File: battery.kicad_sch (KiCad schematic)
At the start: 22 parts, among them J1 Conn_01x04_Female, J10 Conn_01x06_Male, J11 Conn_01x02_Female, J2 Conn_02x05_Odd_Even, J3 Conn_02x03_Odd_Even, Q1 2N7002, Q10 Q_PMOS_GSD, Q2 Q_PMOS_GSD, U1 AP3428

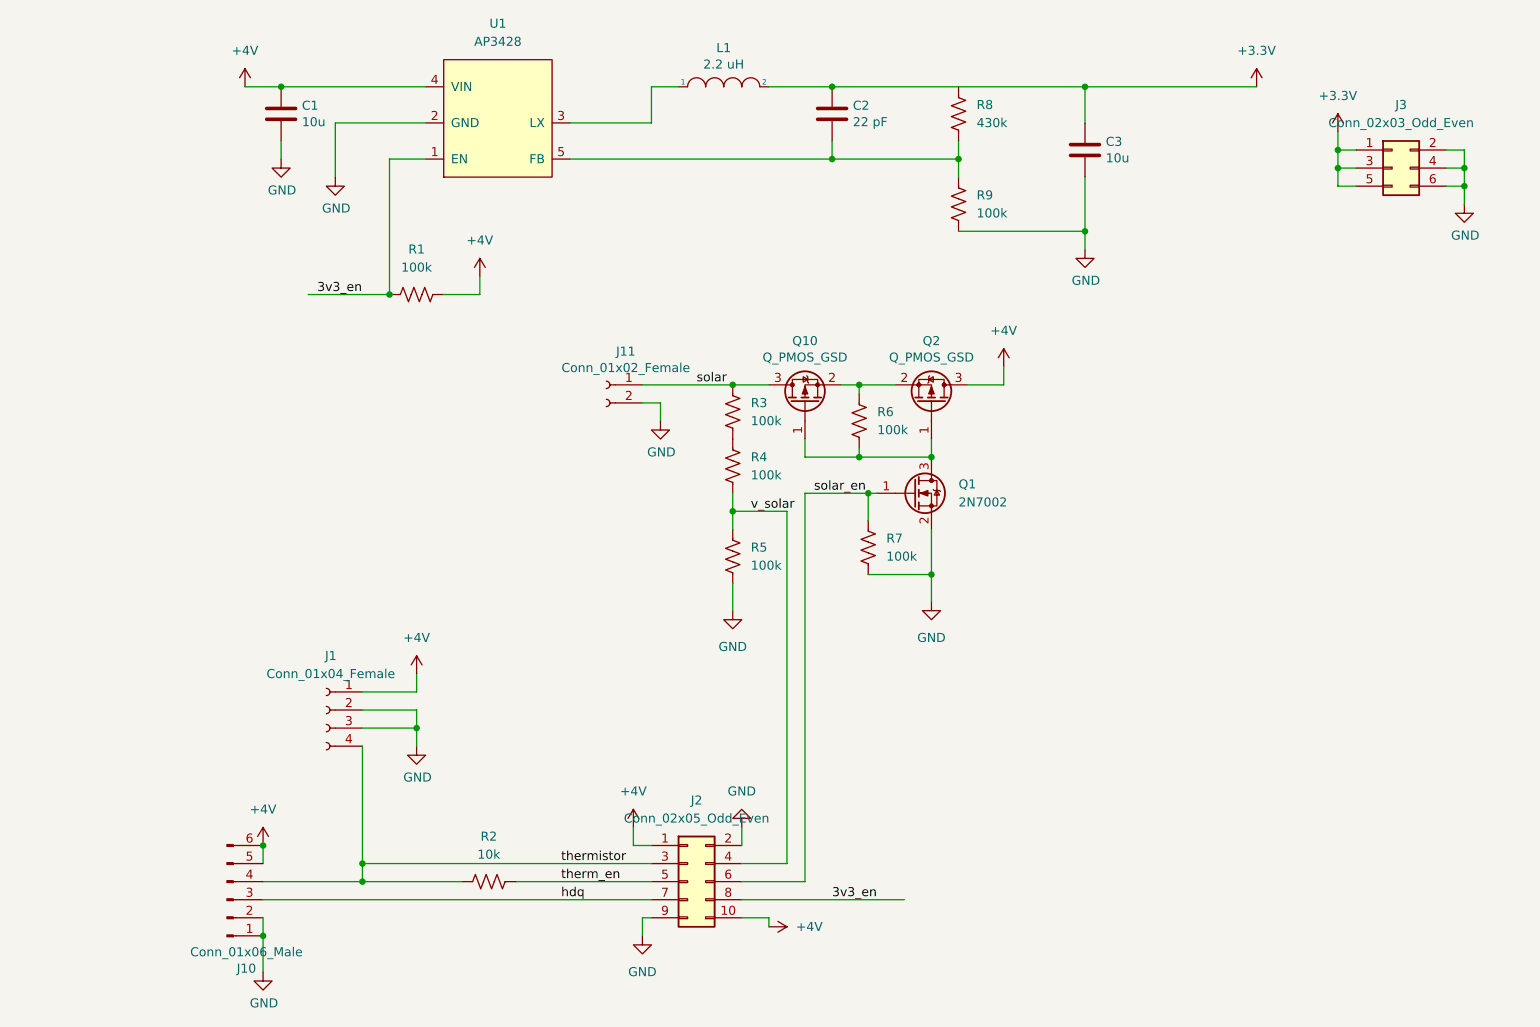
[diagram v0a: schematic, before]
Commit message: tight regulator layout
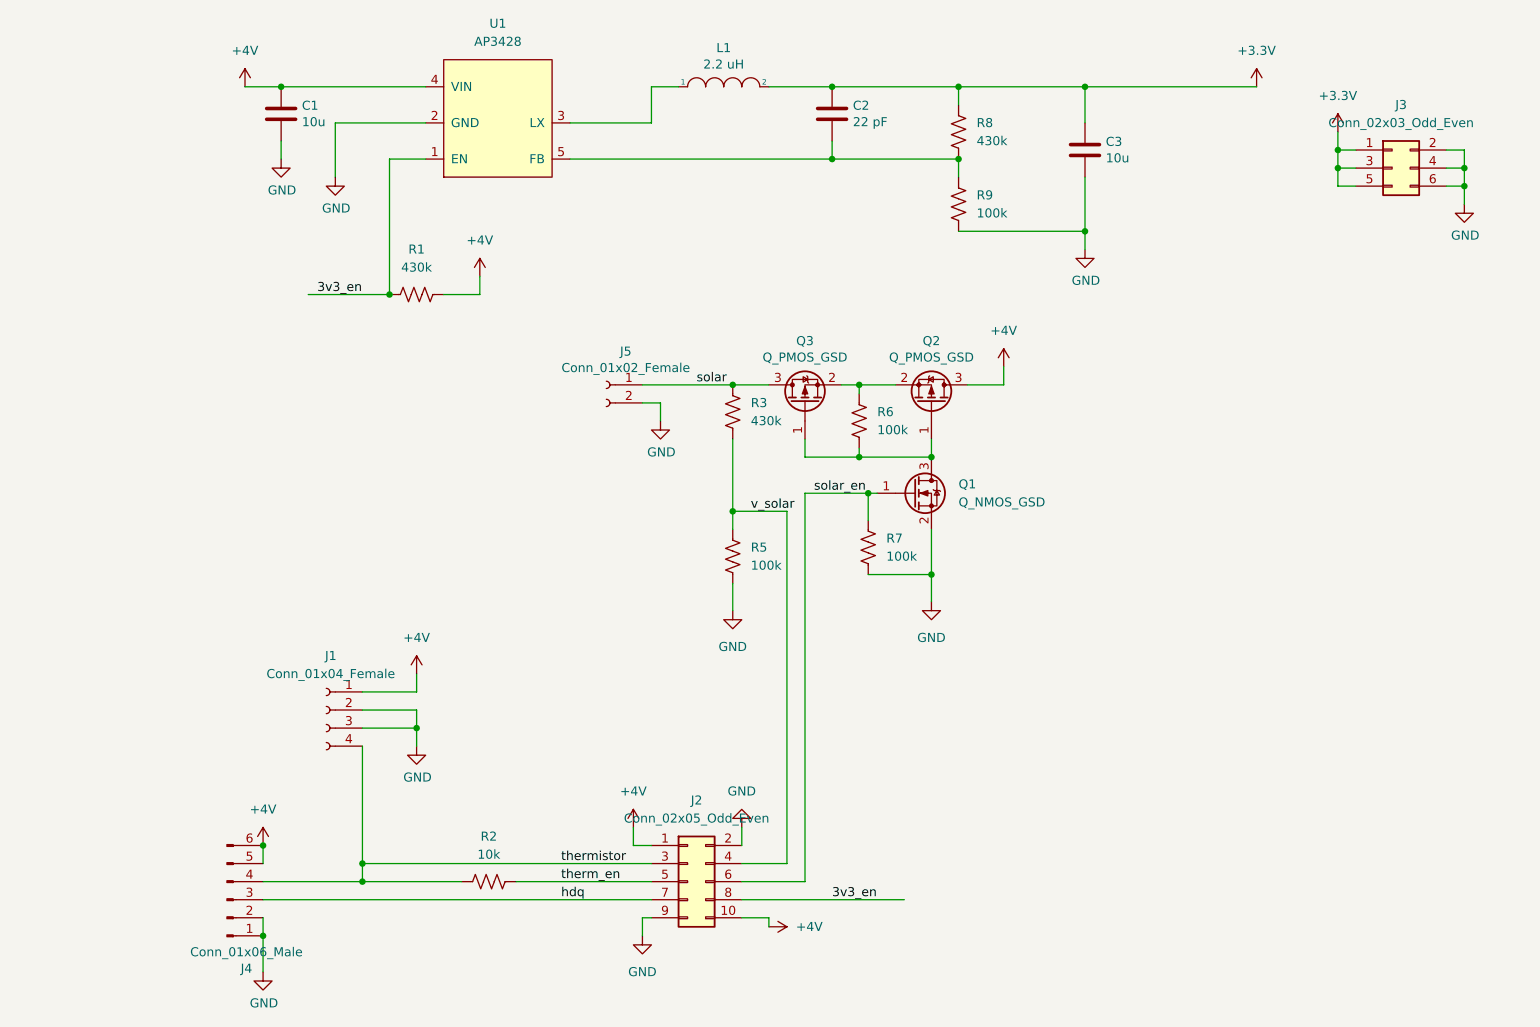
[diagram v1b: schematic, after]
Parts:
- removed Q1: 2N7002, Package_TO_SOT_SMD:SOT-23, symbol Transistor_FET:2N7002
- removed R4: 100k, Resistor_SMD:R_0603_1608Metric, symbol Device:R_US
- added Q1: Q_NMOS_GSD, Package_TO_SOT_SMD:SOT-23, symbol Device:Q_NMOS_GSD
- C1, C3: footprint Capacitors_SMD:C_0805 -> Capacitor_SMD:C_0805_2012Metric
- C2: footprint Capacitors_SMD:C_0603 -> Capacitor_SMD:C_0603_1608Metric
- J5: renamed from J11; footprint Pin_Headers:Pin_Header_Straight_2x01_Pitch2.54mm -> Connector_PinSocket_2.54mm:PinSocket_1x02_P2.54mm_Vertical
- Q2: footprint TO_SOT_Packages_SMD:SOT-23 -> Package_TO_SOT_SMD:SOT-23
- Q3: renamed from Q10; footprint TO_SOT_Packages_SMD:SOT-23 -> Package_TO_SOT_SMD:SOT-23
- R1, R3: value 100k -> 430k
- renumbered J10 to J4
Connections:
- net +3V3: now also R8.1
- net GND: now also Q1.2 (S)
- net solar_en: now also Q1.1 (G)
- net v_solar: now also R3.2
- net at Q2.1 (G), Q3.1 (G), R6.2: now also Q1.3 (D)
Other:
- moved on the sheet: R8

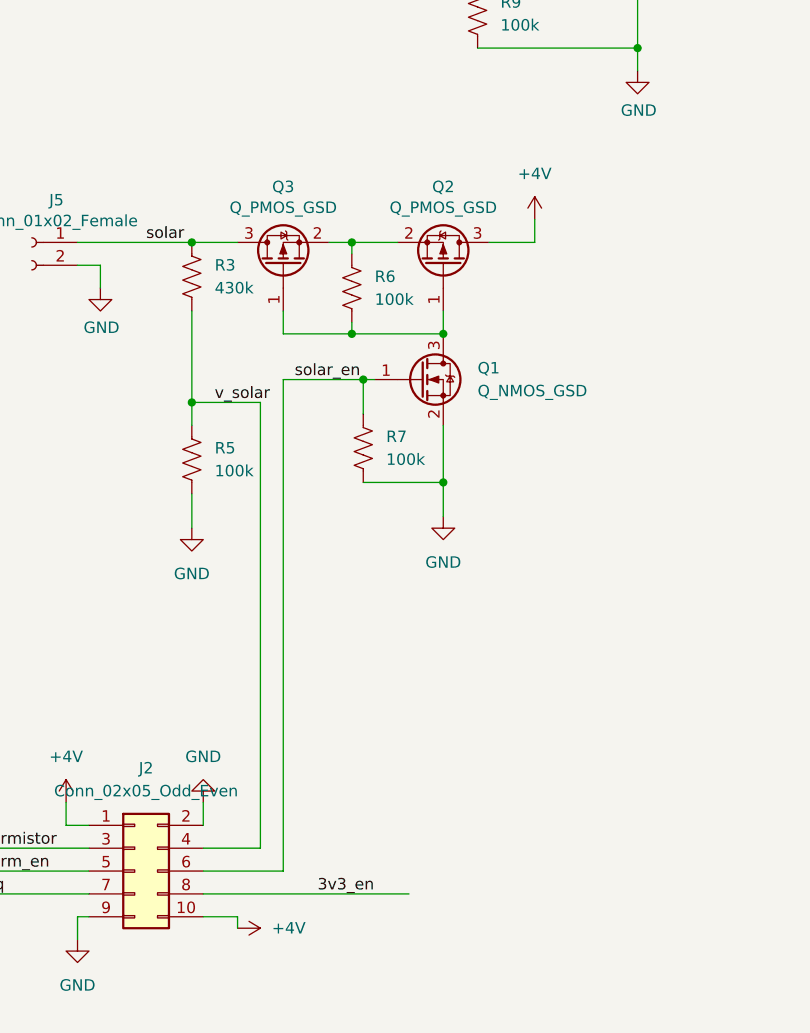
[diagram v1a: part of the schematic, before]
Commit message: High-side switch for solar cell.
Need to place the uC interconnect - maybe a surface-mount connector will
do
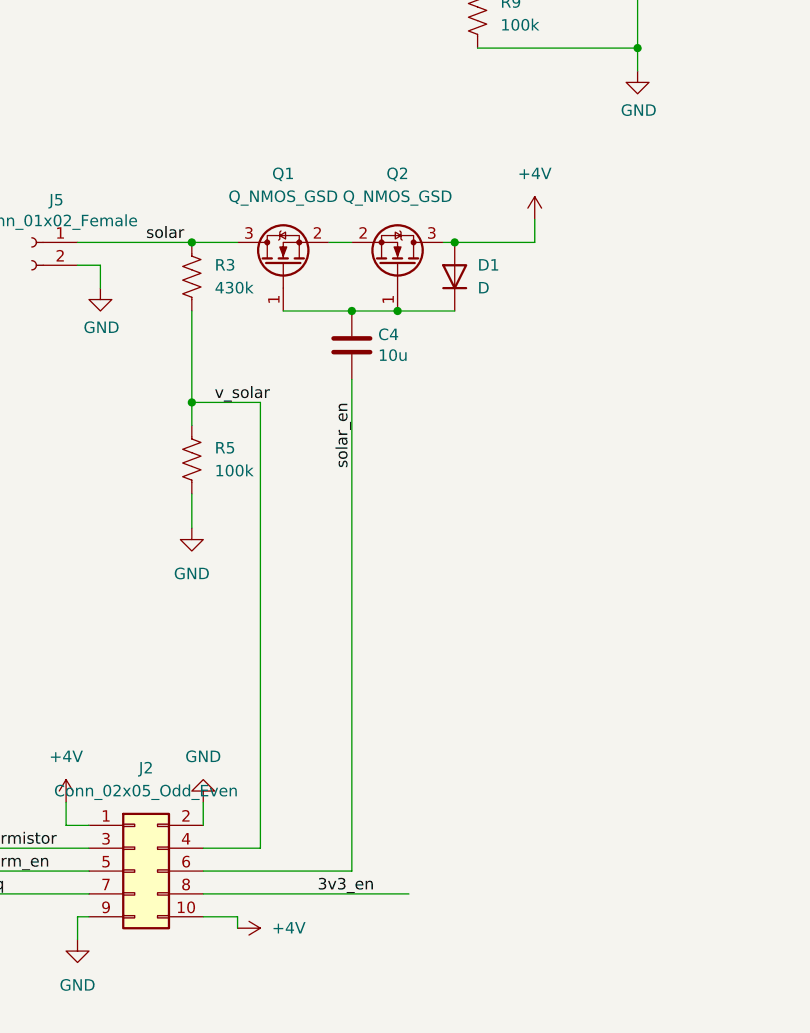
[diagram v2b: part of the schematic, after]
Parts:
- removed Q2, Q3: Q_PMOS_GSD, Package_TO_SOT_SMD:SOT-23, symbol Device:Q_PMOS_GSD
- removed R6, R7: 100k, Resistor_SMD:R_0603_1608Metric, symbol Device:R_US
- added C4: 10u, Capacitor_SMD:C_0805_2012Metric, symbol Device:C
- added D1: D, Diode_SMD:D_SOD-323, symbol Device:D
- added Q2: Q_NMOS_GSD, Package_TO_SOT_SMD:SOT-23, symbol Device:Q_NMOS_GSD
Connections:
- net +4V: now also D1.2 (A), Q2.3 (D)
- net GND: no longer Q1.2 (S)
- net solar: now also Q1.3 (D)
- net solar_en: now also C4.2; no longer Q1.1 (G)
- new net: C4.1, D1.1 (K), Q1.1 (G), Q2.1 (G)
- new net: Q1.2 (S), Q2.2 (S)
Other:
- moved on the sheet: Q1

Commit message: Routed uC interconnect
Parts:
- J2: footprint Connector_PinHeader_2.54mm:PinHeader_2x05_P2.54mm_Vertical -> Connector_PinHeader_2.54mm:PinHeader_2x05_P2.54mm_Vertical_SMD
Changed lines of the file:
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@@
     (property "Reference" "J2" (id 0) (at 133.35 129.54 0))
     (property "Value" "Conn_02x05_Odd_Even" (id 1) (at 133.35 132.08 0))
-    (property "Footprint" "Connector_PinHeader_2.54mm:PinHeader_2x05_P2.54mm_Vertical" (id 2) (at 132.08 140.97 0)
+    (property "Footprint" "Connector_PinHeader_2.54mm:PinHeader_2x05_P2.54mm_Vertical_SMD" (id 2) (at 132.08 140.97 0)
       (effects (font (size 1.27 1.27)) hide)
     )
@@
     )
     (path "/95217bc0-7de8-4cca-b06e-7874ac6e18ee"
-      (reference "J2") (unit 1) (value "Conn_02x05_Odd_Even") (footprint "Connector_PinHeader_2.54mm:PinHeader_2x05_P2.54mm_Vertical")
+      (reference "J2") (unit 1) (value "Conn_02x05_Odd_Even") (footprint "Connector_PinHeader_2.54mm:PinHeader_2x05_P2.54mm_Vertical_SMD")
     )
     (path "/dce5a116-755b-4b06-94a3-2ca0fb373483"

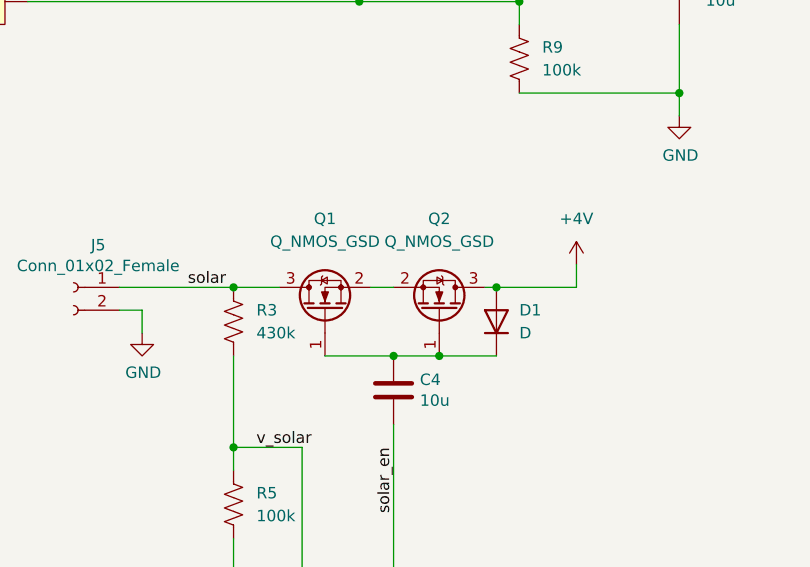
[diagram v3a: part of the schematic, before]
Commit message: Changed to single transistor for solar disconnect
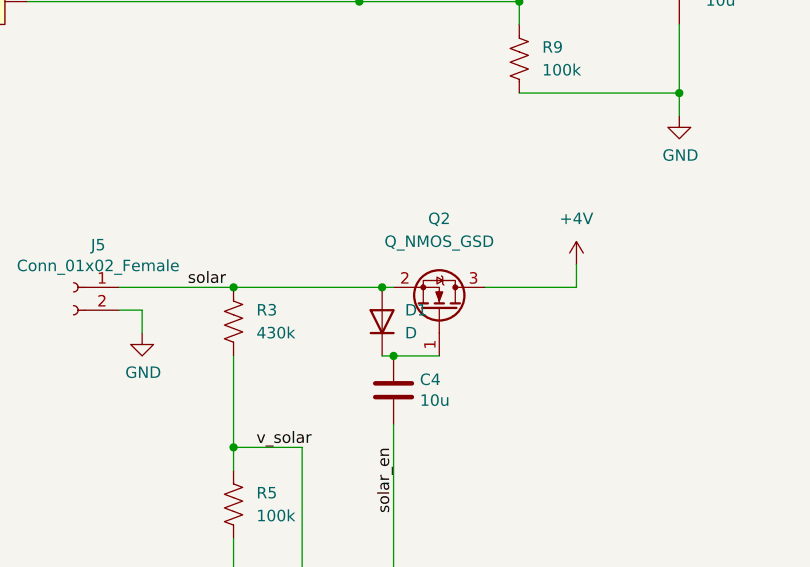
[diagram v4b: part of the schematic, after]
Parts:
- removed Q1: Q_NMOS_GSD, Package_TO_SOT_SMD:SOT-23, symbol Device:Q_NMOS_GSD
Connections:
- net +4V: no longer D1.2 (A)
- net solar: now also D1.2 (A), Q2.2 (S)
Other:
- moved on the sheet: D1
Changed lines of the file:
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@@
   (junction (at 152.4 29.21) (diameter 0) (color 0 0 0 0)
   )
-  (junction (at 167.64 71.12) (diameter 0) (color 0 0 0 0)
-  )
   (junction (at 241.3 40.64) (diameter 0) (color 0 0 0 0)
   )
+  (junction (at 154.94 71.12) (diameter 0) (color 0 0 0 0)
+  )
   (junction (at 187.96 29.21) (diameter 0) (color 0 0 0 0)
   )
@@
   (junction (at 223.52 40.64) (diameter 0) (color 0 0 0 0)
   )
-  (junction (at 161.29 78.74) (diameter 0) (color 0 0 0 0)
-  )
   (junction (at 86.36 140.97) (diameter 0) (color 0 0 0 0)
   )
@@
     (stroke (width 0) (type default) (color 0 0 0 0))
   )
-  (wire (pts (xy 161.29 78.74) (xy 167.64 78.74))
-    (stroke (width 0) (type default) (color 0 0 0 0))
-  )
   (wire (pts (xy 143.51 146.05) (xy 139.7 146.05))
     (stroke (width 0) (type default) (color 0 0 0 0))
@@
     (stroke (width 0) (type default) (color 0 0 0 0))
   )
-  (wire (pts (xy 138.43 71.12) (xy 143.51 71.12))
+  (wire (pts (xy 138.43 71.12) (xy 154.94 71.12))
     (stroke (width 0) (type default) (color 0 0 0 0))
   )
@@
     (stroke (width 0) (type default) (color 0 0 0 0))
   )
+  (wire (pts (xy 154.94 71.12) (xy 156.21 71.12))
+    (stroke (width 0) (type default) (color 0 0 0 0))
+  )
   (wire (pts (xy 241.3 43.18) (xy 241.3 40.64))
     (stroke (width 0) (type default) (color 0 0 0 0))
@@
     (stroke (width 0) (type default) (color 0 0 0 0))
   )
-  (wire (pts (xy 153.67 71.12) (xy 156.21 71.12))
-    (stroke (width 0) (type default) (color 0 0 0 0))
-  )
   (wire (pts (xy 156.21 78.74) (xy 161.29 78.74))
     (stroke (width 0) (type default) (color 0 0 0 0))
@@
     (stroke (width 0) (type default) (color 0 0 0 0))
   )
+  (wire (pts (xy 154.94 78.74) (xy 156.21 78.74))
+    (stroke (width 0) (type default) (color 0 0 0 0))
+  )
   (wire (pts (xy 78.74 58.42) (xy 90.17 58.42))
     (stroke (width 0) (type default) (color 0 0 0 0))
@@
     (stroke (width 0) (type default) (color 0 0 0 0))
   )
-  (wire (pts (xy 167.64 71.12) (xy 176.53 71.12))
+  (wire (pts (xy 166.37 71.12) (xy 176.53 71.12))
     (stroke (width 0) (type default) (color 0 0 0 0))
   )
@@
     (stroke (width 0) (type default) (color 0 0 0 0))
   )
-  (wire (pts (xy 148.59 78.74) (xy 156.21 78.74))
-    (stroke (width 0) (type default) (color 0 0 0 0))
-  )
   (wire (pts (xy 102.87 58.42) (xy 97.79 58.42))
     (stroke (width 0) (type default) (color 0 0 0 0))
@@
   )
   (wire (pts (xy 238.76 40.64) (xy 241.3 40.64))
-    (stroke (width 0) (type default) (color 0 0 0 0))
-  )
-  (wire (pts (xy 166.37 71.12) (xy 167.64 71.12))
     (stroke (width 0) (type default) (color 0 0 0 0))
   )
@@
     (pin "3")
     (pin "4")
-  )
-  (symbol (lib_id "Device:Q_NMOS_GSD") (at 148.59 73.66 90) (unit 1)
-    (in_bom yes) (on_board yes) (fields_autoplaced)
-    (property "Reference" "Q1" (id 0) (at 148.59 63.5 90))
-    (property "Value" "Q_NMOS_GSD" (id 1) (at 148.59 66.04 90))
-    (property "Footprint" "Package_TO_SOT_SMD:SOT-23" (id 2) (at 146.05 68.58 0)
-      (effects (font (size 1.27 1.27)) hide)
-    )
-    (property "Datasheet" "https://media.digikey.com/pdf/Data%20Sheets/Rohm%20PDFs/RUC002N05HZGT116_Rev.001_6-6-16.pdf" (id 3) (at 148.59 73.66 0)
-      (effects (font (size 1.27 1.27)) hide)
-    )
-    (pin "1")
-    (pin "2")
-    (pin "3")
   )
   (symbol (lib_id "Device:R_US") (at 170.18 45.72 0) (unit 1)
@@
     (pin "2")
   )
-  (symbol (lib_id "Device:D") (at 167.64 74.93 90) (unit 1)
-    (in_bom yes) (on_board yes) (fields_autoplaced)
-    (property "Reference" "D1" (id 0) (at 170.18 73.6599 90)
+  (symbol (lib_id "Device:D") (at 154.94 74.93 90) (unit 1)
+    (in_bom yes) (on_board yes) (fields_autoplaced)
+    (property "Reference" "D1" (id 0) (at 157.48 73.6599 90)
       (effects (font (size 1.27 1.27)) (justify right))
     )
-    (property "Value" "D" (id 1) (at 170.18 76.1999 90)
+    (property "Value" "D" (id 1) (at 157.48 76.1999 90)
       (effects (font (size 1.27 1.27)) (justify right))
     )
-    (property "Footprint" "Diode_SMD:D_SOD-323" (id 2) (at 167.64 74.93 0)
-      (effects (font (size 1.27 1.27)) hide)
-    )
-    (property "Datasheet" "https://toshiba.semicon-storage.com/info/docget.jsp?did=3342&prodName=1SS367" (id 3) (at 167.64 74.93 0)
+    (property "Footprint" "Diode_SMD:D_SOD-323" (id 2) (at 154.94 74.93 0)
+      (effects (font (size 1.27 1.27)) hide)
+    )
+    (property "Datasheet" "https://toshiba.semicon-storage.com/info/docget.jsp?did=3342&prodName=1SS367" (id 3) (at 154.94 74.93 0)
       (effects (font (size 1.27 1.27)) hide)
     )
@@
       (reference "L1") (unit 1) (value "2.2 uH") (footprint "Inductor_SMD:L_0805_2012Metric")
     )
-    (path "/2090f974-bc50-4e96-91ce-fb27aacf7edf"
-      (reference "Q1") (unit 1) (value "Q_NMOS_GSD") (footprint "Package_TO_SOT_SMD:SOT-23")
-    )
     (path "/3ea0585c-7a8e-4d46-bf74-06325b501cab"
